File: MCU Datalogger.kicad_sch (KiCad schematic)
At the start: 25 parts, among them U1 24LC1025, U2 DS1337S_, U3 24LC1025, U4 ATMEGA328P-AU, Y1 32.768 KHz, Y2 16 MHz

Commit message: Test.
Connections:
- net at Y1.1: now also U2.2 (X2)
- net at Y1.2: now also U2.1 (X1)
- net at C5.1: now also BT1.1 (+), D2.2 (A), U4.18 (AVCC), U4.4 (VCC)
- net GND: now reaches C5.2
- net GND: now also BT1.2 (-), C1.2, C2.1, C3.1, C4.1, R5.1, R7.2, U1.4 (GND), U1.7 (WP), U2.4 (GND), U3.2 (A1), U3.4 (GND), U3.7 (WP), U4.21 (GND), U4.3 (GND), U4.5 (GND)
- net Vcc: now reaches R1.1
- net Vcc: now also C1.1, R2.1, R3.1, R4.1, R6.1, U1.1 (A0), U1.2 (A1), U1.3 (A2), U1.8 (VCC), U2.8 (VCC), U3.1 (A0), U3.3 (A2), U3.8 (VCC)
- net at R1.2: now also U2.3 (~{INTA})
- net at R7.1: now also D2.1 (K)
- net RESET: now reaches R6.2
- net RESET: now also U4.29 (PC6/~{RESET})
- net at C3.2: now also U4.8 (PB7), Y2.1
- net at C2.2: now also U4.7 (PB6), Y2.2
- net SDA: now reaches U2.5 (SDA)
- net SDA: now also R4.2, U1.5 (SDA), U3.5 (SDA), U4.27 (PC4)
- net SCK: now reaches U2.6 (SCL)
- net SCK: now also D1.2 (A), R3.2, U1.6 (SCL), U3.6 (SCL), U4.17 (PB5), U4.28 (PC5)
- net at U2.7 (SQW/~INT): now also R2.2
- net at C4.2: now also U4.20 (AREF)
- net D3: now reaches U4.1 (PD3)
- net D6: now reaches U4.10 (PD6)
- net D7: now reaches U4.11 (PD7)
- net D8: now reaches U4.12 (PB0)
- net MOSI: now reaches U4.15 (PB3)
- net MISO: now reaches U4.16 (PB4)
- net D4: now reaches U4.2 (PD4)
- net RX: now reaches U4.30 (PD0)
- net TX: now reaches U4.31 (PD1)
- net D2: now reaches U4.32 (PD2)
- net at U4.6 (VCC): no longer U4.4 (VCC)
- net D5: now reaches U4.9 (PD5)
- net at R5.2: now also D1.1 (K)
- no-connect marks 0 -> 9
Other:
- moved on the sheet: BT1, C2, C3, C4, C5, D1, D2, R1, R2, R4, R5, R6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

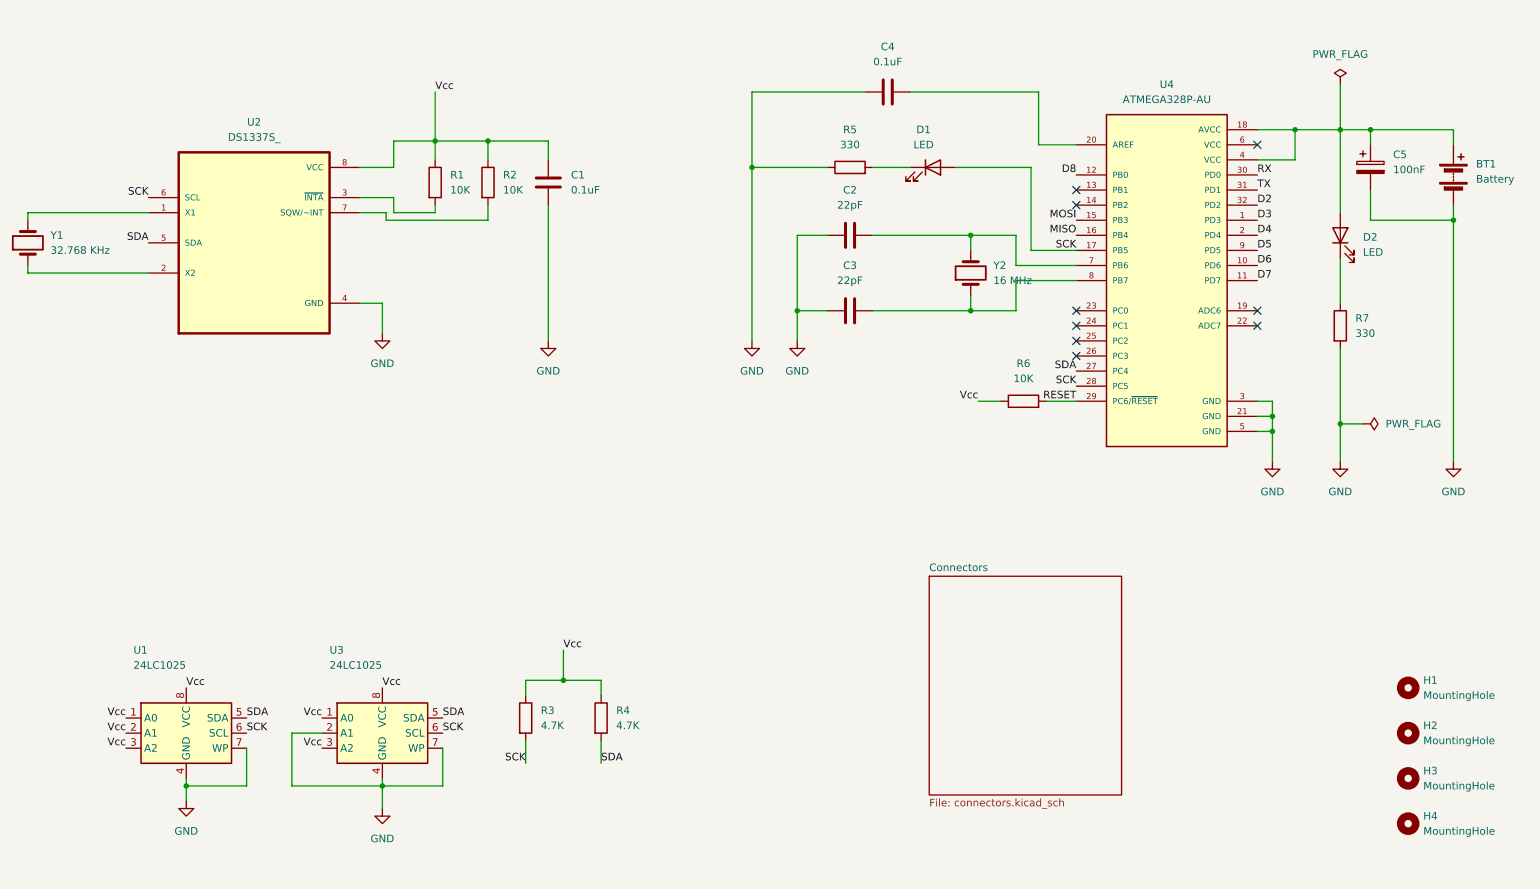
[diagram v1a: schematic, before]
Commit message: Completed wiring in the second sheet.
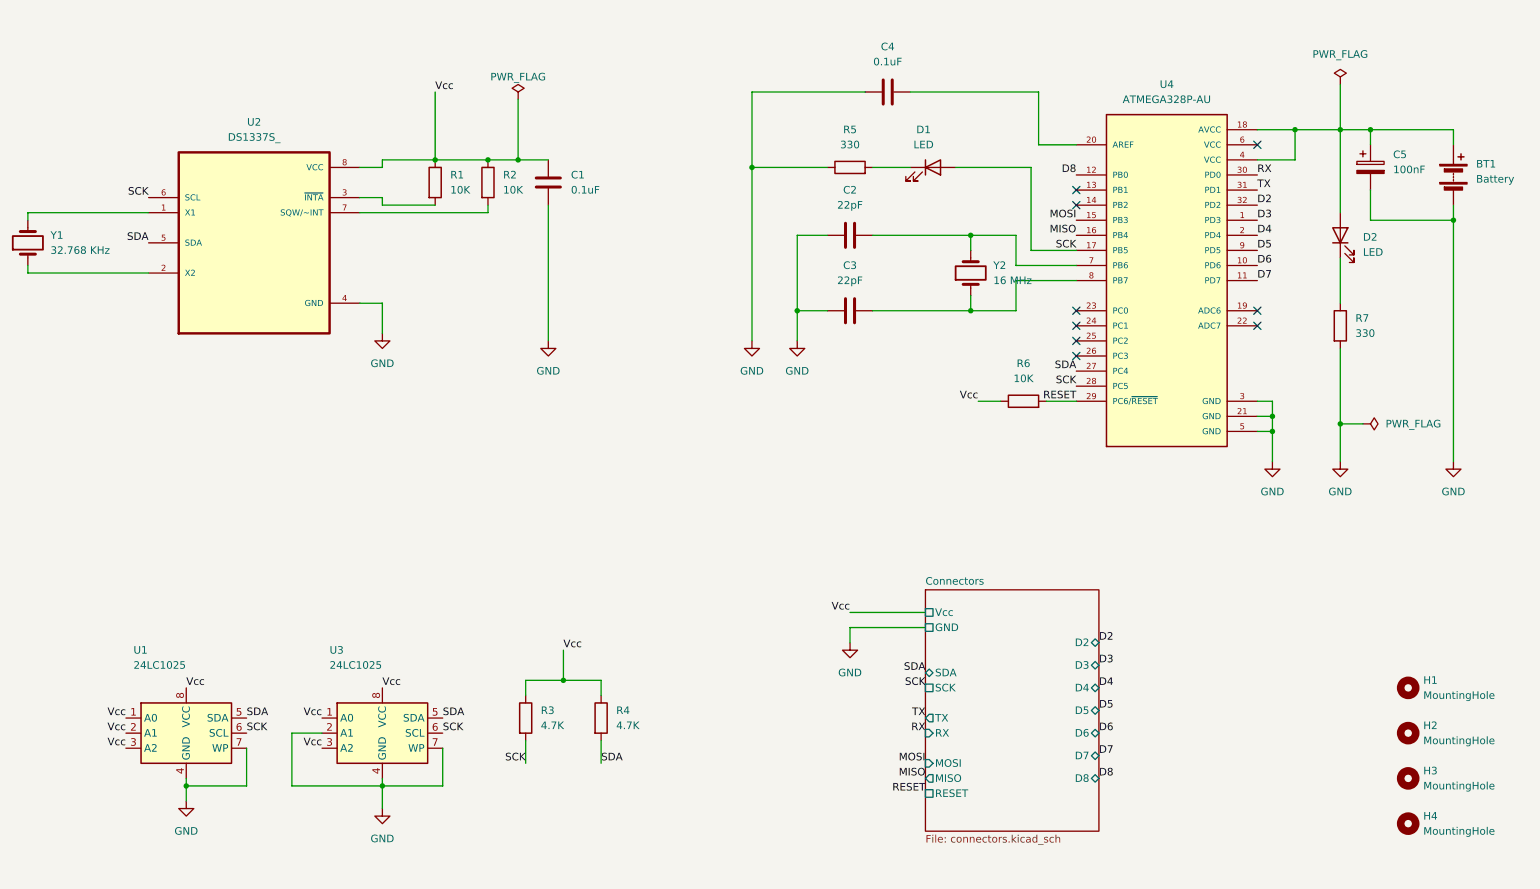
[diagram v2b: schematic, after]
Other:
- sheet Connectors ports: added D2, D3, D4, D5, D6, D7, D8, GND, MISO, MOSI, RESET, RX, SCK, SDA, TX, Vcc; removed none

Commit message: Added comments.
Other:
- note added: "EEPROM"
- note added: "MCU"
- note added: "Mounting"
- note added: "Real time clock"
- moved on the sheet: C1, H1, H2, H3, H4, R1, R2, R3, R4, U1, U2, U3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

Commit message: Fix outstanding issues.
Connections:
- net Vcc: now also BT1.1 (+), C5.1, D2.2 (A), U4.18 (AVCC), U4.4 (VCC)
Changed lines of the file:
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@@
+	(wire
+		(pts
+			(xy 251.46 39.37) (xy 265.43 39.37)
+		)
+		(stroke
+			(width 0)
+			(type default)
+		)
+	)
 	(wire
 		(pts
@@
 		(pts
 			(xy 101.6 43.18) (xy 110.49 43.18)
-		)
-		(stroke
-			(width 0)
-			(type default)
-		)
-	)
-	(wire
-		(pts
-			(xy 265.43 39.37) (xy 251.46 39.37)
 		)
 		(stroke
@@
 		(fields_autoplaced yes)
 		(effects
+			(font
+				(size 1.27 1.27)
+			)
+			(justify left bottom)
+		)
+	)
+	(label "Vcc"
+		(at 256.54 39.37 0)
+		(fields_autoplaced yes)
+		(effects

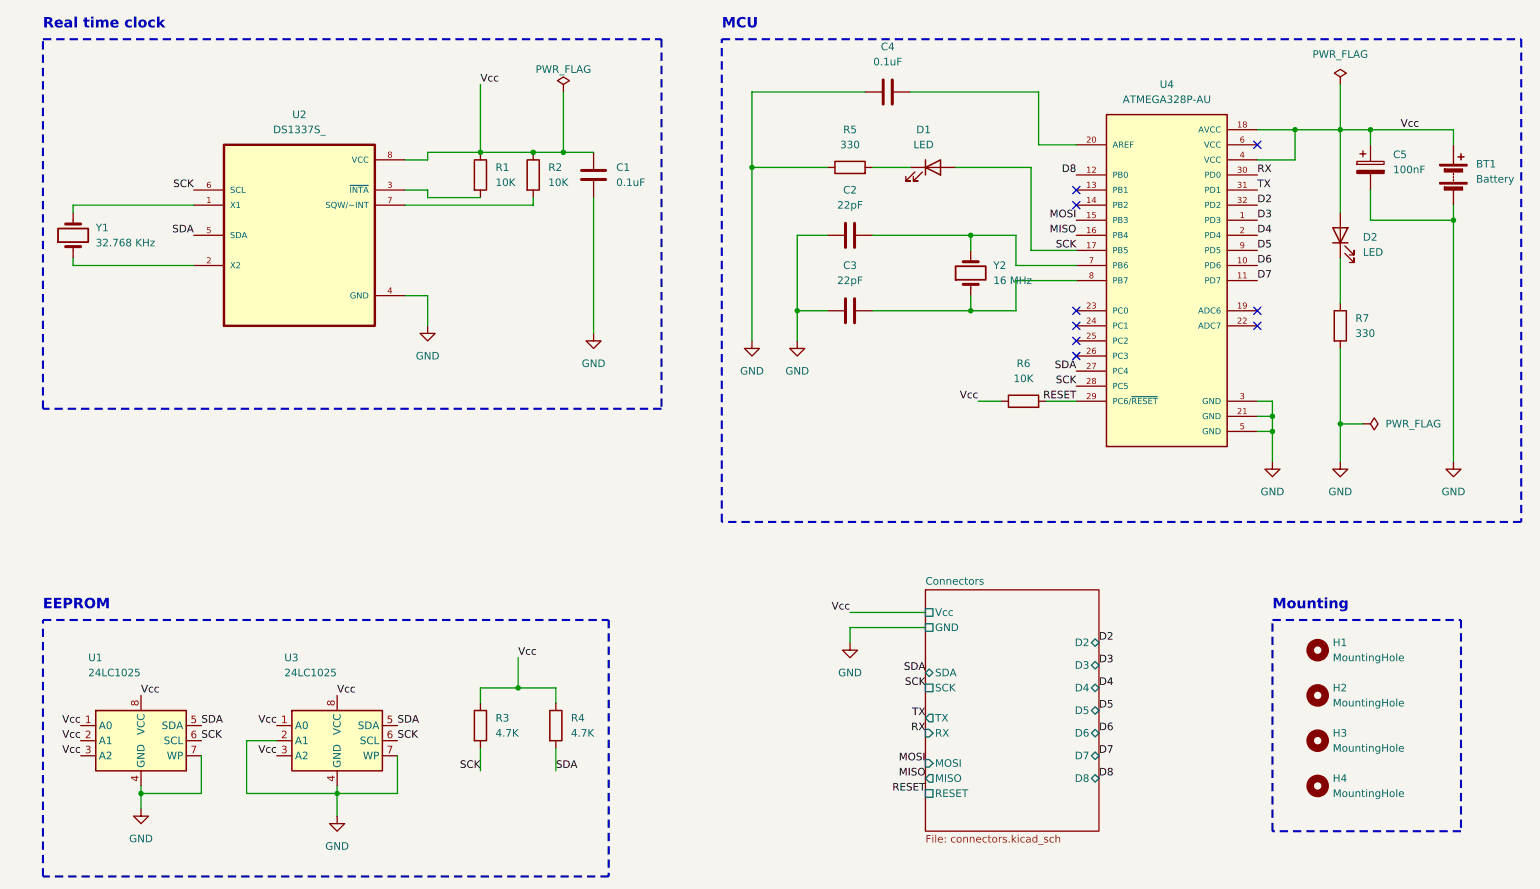
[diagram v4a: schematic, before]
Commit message: Fixed two defects in the schematic.
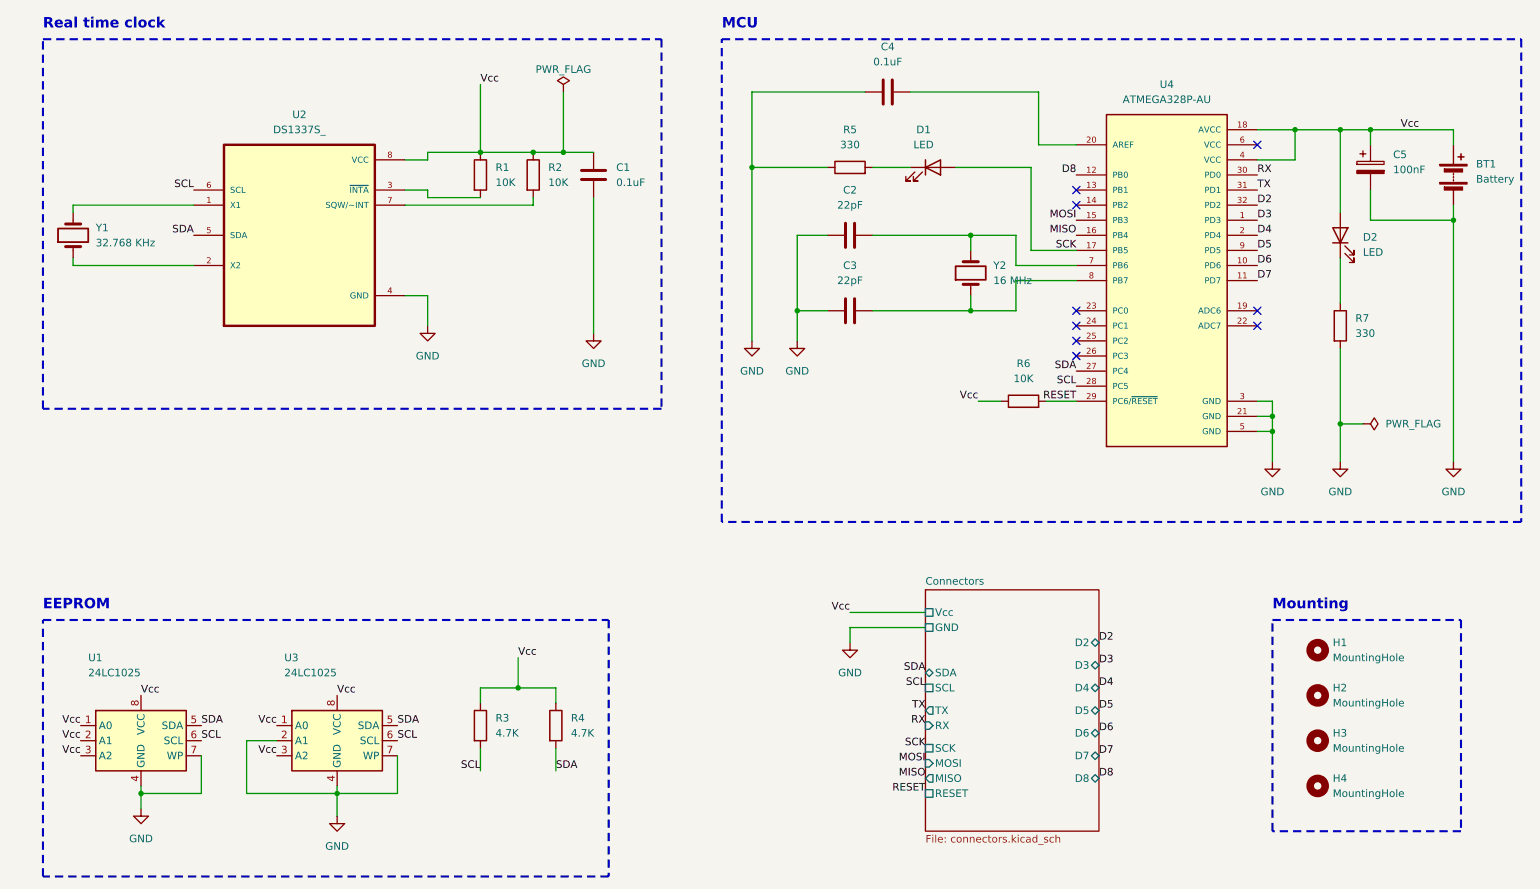
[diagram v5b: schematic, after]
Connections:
- net SCK: no longer R3.2, U1.6 (SCL), U2.6 (SCL), U3.6 (SCL), U4.28 (PC5)
- new net SCL: R3.2, U1.6 (SCL), U2.6 (SCL), U3.6 (SCL), U4.28 (PC5)
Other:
- sheet Connectors ports: added SCL; removed none
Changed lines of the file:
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@@
 	(wire
 		(pts
-			(xy 246.38 31.75) (xy 246.38 39.37)
-		)
-		(stroke
-			(width 0)
-			(type default)
-		)
-	)
-	(wire
-		(pts
 			(xy 232.41 87.63) (xy 234.95 87.63)
 		)
@@
 		)
 	)
+	(label "SCK"
+		(at 176.53 143.51 180)
+		(fields_autoplaced yes)
+		(effects
+			(font
+				(size 1.27 1.27)
+			)
+			(justify right bottom)
+		)
+	)
 	(label "RX"
 		(at 232.41 46.99 0)
@@
 		)
 	)
-	(label "SCK"
-		(at 101.6 147.32 180)
+	(label "SCL"
+		(at 176.53 133.35 180)
 		(fields_autoplaced yes)
 		(effects
@@
 	)
 	(label "RX"
-		(at 176.53 140.97 180)
+		(at 176.53 139.7 180)
 		(fields_autoplaced yes)
 		(effects
@@
 	)
 	(label "SCK"
-		(at 87.63 142.24 0)
-		(fields_autoplaced yes)
-		(effects
-			(font
-				(size 1.27 1.27)
-			)
-			(justify left bottom)
-		)
-	)
-	(label "SCK"
 		(at 201.93 59.69 180)
 		(fields_autoplaced yes)
@@
 		)
 	)
-	(label "SCK"
-		(at 176.53 133.35 180)
-		(fields_autoplaced yes)
-		(effects
-			(font
-				(size 1.27 1.27)
-			)
-			(justify right bottom)
-		)
-	)
 	(label "D6"
 		(at 232.41 62.23 0)
@@
 		)
 	)
+	(label "SCL"
+		(at 54.61 142.24 0)
+		(fields_autoplaced yes)
+		(effects
+			(font
+				(size 1.27 1.27)
+			)
+			(justify left bottom)
+		)
+	)
+	(label "SCL"
+		(at 101.6 147.32 180)
+		(fields_autoplaced yes)
+		(effects
+			(font
+				(size 1.27 1.27)
+			)
+			(justify right bottom)
+		)
+	)
+	(label "SCL"
+		(at 87.63 142.24 0)
+		(fields_autoplaced yes)
+		(effects
+			(font
+				(size 1.27 1.27)
+			)
+			(justify left bottom)
+		)
+	)
 	(label "Vcc"
 		(at 44.45 134.62 0)
@@
 		)
 	)
-	(label "SCK"
+	(label "SCL"
 		(at 201.93 82.55 180)
 		(fields_autoplaced yes)
@@
 	)
 	(label "TX"
-		(at 176.53 138.43 180)
+		(at 176.53 137.16 180)
 		(fields_autoplaced yes)
 		(effects
@@
 		)
 	)
-	(label "Vcc"
-		(at 67.31 144.78 180)
+	(label "SCL"
+		(at 53.34 49.53 180)
 		(fields_autoplaced yes)
 		(effects
@@
 		)
 	)
-	(label "SCK"
-		(at 53.34 49.53 180)
+	(label "Vcc"
+		(at 67.31 144.78 180)
 		(fields_autoplaced yes)
 		(effects
@@
 		)
 	)
-	(label "SCK"
-		(at 54.61 142.24 0)
-		(fields_autoplaced yes)
-		(effects
-			(font
-				(size 1.27 1.27)
-			)
-			(justify left bottom)
-		)
-	)
 	(label "Vcc"
 		(at 185.42 85.09 180)
@@
 	)
 	(symbol
-		(lib_id "power:PWR_FLAG")
-		(at 246.38 31.75 0)
-		(unit 1)
-		(exclude_from_sim no)
-		(in_bom yes)
-		(on_board yes)
-		(dnp no)
-		(fields_autoplaced yes)
-		(property "Reference" "#FLG01"
-			(at 246.38 29.845 0)
-			(effects
-				(font
-					(size 1.27 1.27)
-				)
-				(hide yes)
-			)
-		)
-		(property "Value" "PWR_FLAG"
-			(at 246.38 26.67 0)
-			(effects
-				(font
-					(size 1.27 1.27)
-				)
-			)
-		)
-		(property "Footprint" ""
-			(at 246.38 31.75 0)
-			(effects
-				(font
-					(size 1.27 1.27)
-				)
-				(hide yes)
-			)
-		)
-		(property "Datasheet" "~"
-			(at 246.38 31.75 0)
-			(effects
-				(font
-					(size 1.27 1.27)
-				)
-				(hide yes)
-			)
-		)
-		(property "Description" "Special symbol for telling ERC where power comes from"
-			(at 246.38 31.75 0)
-			(effects
-				(font
-					(size 1.27 1.27)
-				)
-				(hide yes)
-			)
-		)
-		(pin "1"
-		)
-		(instances
-			(project ""
-				(path "/eb036d61-982e-41fc-ad07-0dff52d6a1cc"
-					(reference "#FLG01")
-					(unit 1)
-				)
-			)
-		)
-	)
-	(symbol
 		(lib_id "power:GND")
 		(at 154.94 74.93 0)
@@
 			)
 		)
-		(pin "SCK" passive
-			(at 176.53 133.35 180)
-			(effects
-				(font
-					(size 1.27 1.27)
-				)
-				(justify left)
-			)
-		)
 		(pin "GND" passive
 			(at 176.53 123.19 180)
@@
 		)
 		(pin "TX" output
-			(at 176.53 138.43 180)
+			(at 176.53 137.16 180)
 			(effects
 				(font
@@
 		)
 		(pin "RX" input
-			(at 176.53 140.97 180)
+			(at 176.53 139.7 180)
 			(effects
 				(font
@@
 			(effects
 				(font
+					(size 1.27 1.27)
+				)
+				(justify left)
+			)
+		)
+		(pin "SCL" passive
+			(at 176.53 133.35 180)
+			(effects
+				(font
+					(size 1.27 1.27)
+				)
+				(justify left)
+			)
+		)
+		(pin "SCK" passive
+			(at 176.53 143.51 180)
+			(effects
+				(font
